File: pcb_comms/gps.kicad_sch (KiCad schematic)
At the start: 22 parts, among them U1 MAX-M10S-00B

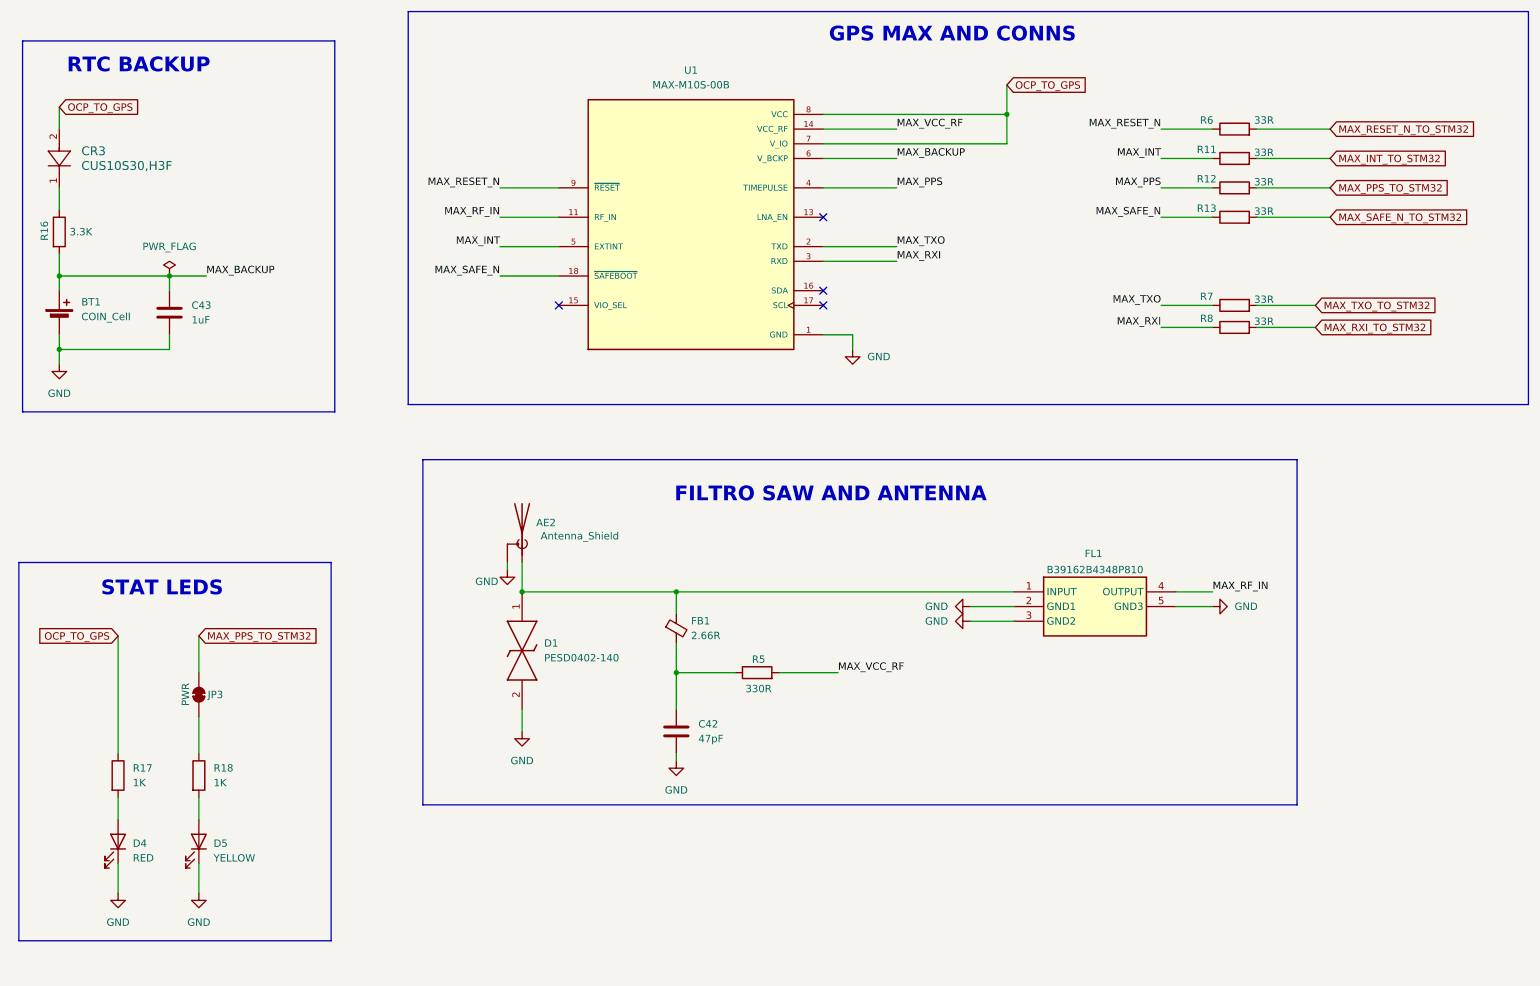
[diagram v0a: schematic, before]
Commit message: Add footprints
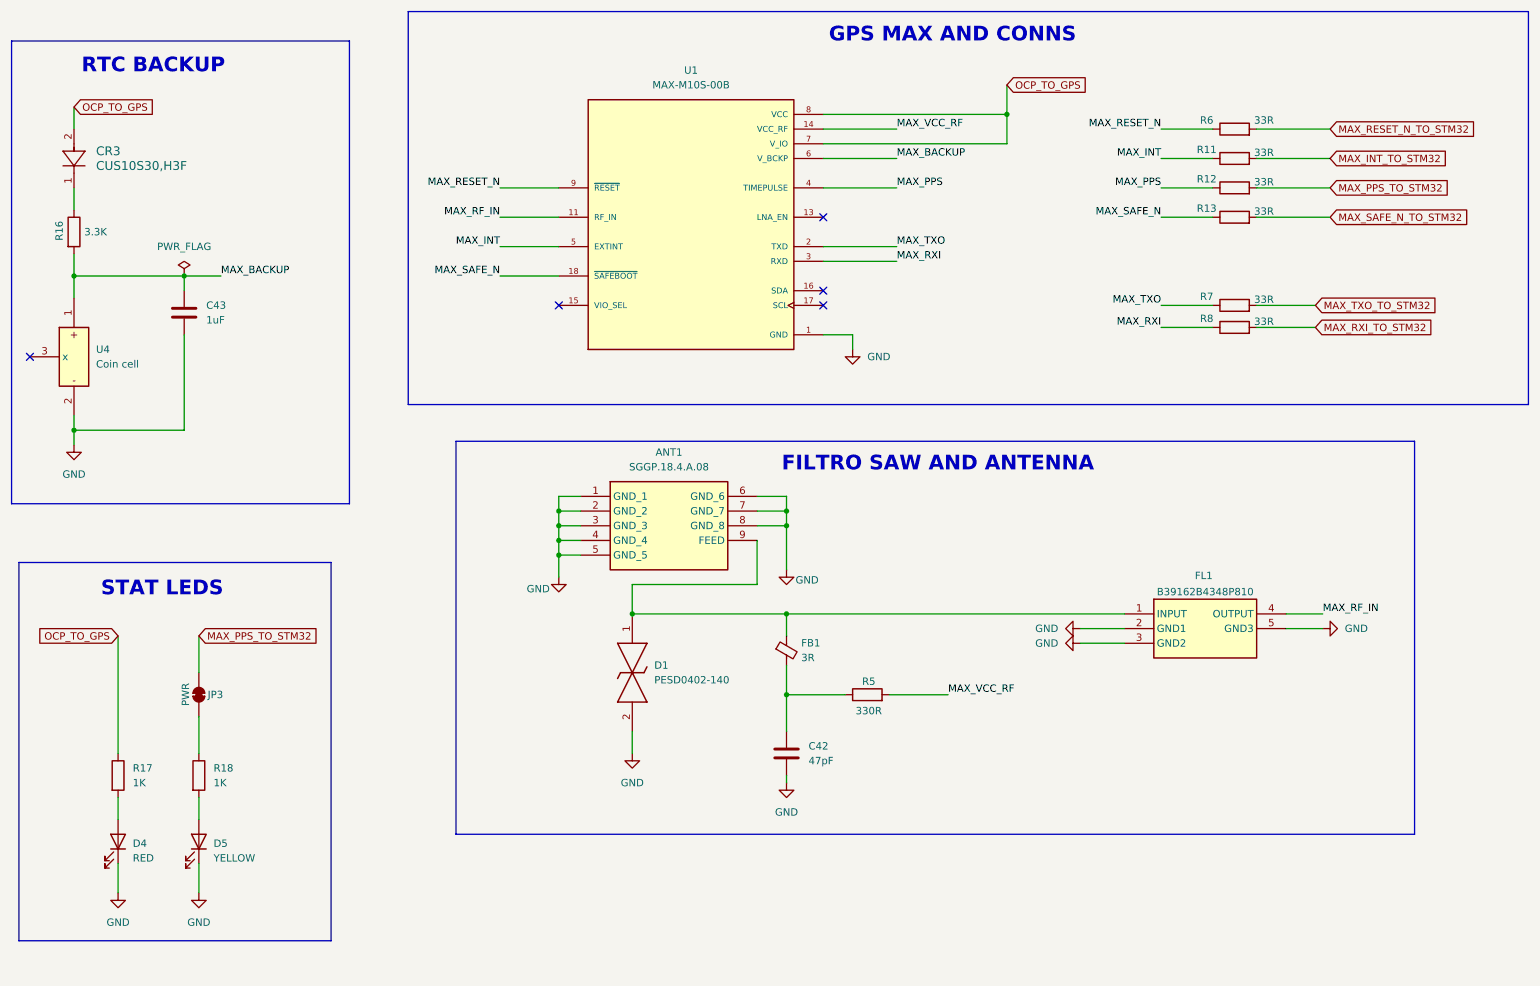
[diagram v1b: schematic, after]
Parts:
- removed AE2: Antenna_Shield, symbol Device:Antenna_Shield
- removed BT1: COIN_Cell, symbol Device:Battery_Cell
- added ANT1: SGGP.18.4.A.08, GPS_Antenna_SGGP.18.4.A.08:GPS_Antenna_SGGP.18.4.A.08, symbol GPS_Antenna_SGGP.18.4.A.08:SGGP.18.4.A.08
- added U4: Coin cell, GPS_BATTERY_HOLDER_2994:GPS_BATTERY_HOLDER_2994, symbol GPS_BATTERY_HOLDER_2994:2994TR
- C42, C43: footprint (none) -> Capacitor_SMD:C_0805_2012Metric_Pad1.18x1.45mm_HandSolder
- CR3: footprint (none) -> SCHOTTKY_DIODE_CUS10S30,H3F:SCHOTTKY_DIODE_CUS10S30,H3F
- D1: footprint (none) -> ESD_PROTECTION_DIODE_PESD0402-140:ESD_PROTECTION_DIODE_PESD0402-140
- D4, D5: footprint (none) -> LED_SMD:LED_0805_2012Metric_Pad1.15x1.40mm_HandSolder
- FB1: value 2.66R -> 3R; footprint (none) -> Inductor_SMD:L_0603_1608Metric_Pad1.05x0.95mm_HandSolder
- FL1: footprint (none) -> GPS_SAW_FILTER:B39162B4348P810
- JP3: footprint (none) -> Jumper:SolderJumper-2_P1.3mm_Bridged_RoundedPad1.0x1.5mm
- R11, R12, R13, R16, R17, R18, R5, R6, R7, R8: footprint (none) -> Resistor_SMD:R_0805_2012Metric_Pad1.20x1.40mm_HandSolder
- U1: footprint (none) -> GPS_MAX_M10S:XCVR_MAX-M10S-00B
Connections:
- net GND: now also ANT1.1 (GND_1), ANT1.2 (GND_2), ANT1.3 (GND_3), ANT1.4 (GND_4), ANT1.5 (GND_5), ANT1.6 (GND_6), ANT1.7 (GND_7), ANT1.8 (GND_8), U4.2
- net MAX_BACKUP: now also U4.1
- net at D1.1, FB1.1, FL1.1 (INPUT): now also ANT1.9 (FEED)
- no-connect marks 4 -> 5
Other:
- moved on the sheet: C42, C43, CR3, D1, FB1, FL1, R16, R5

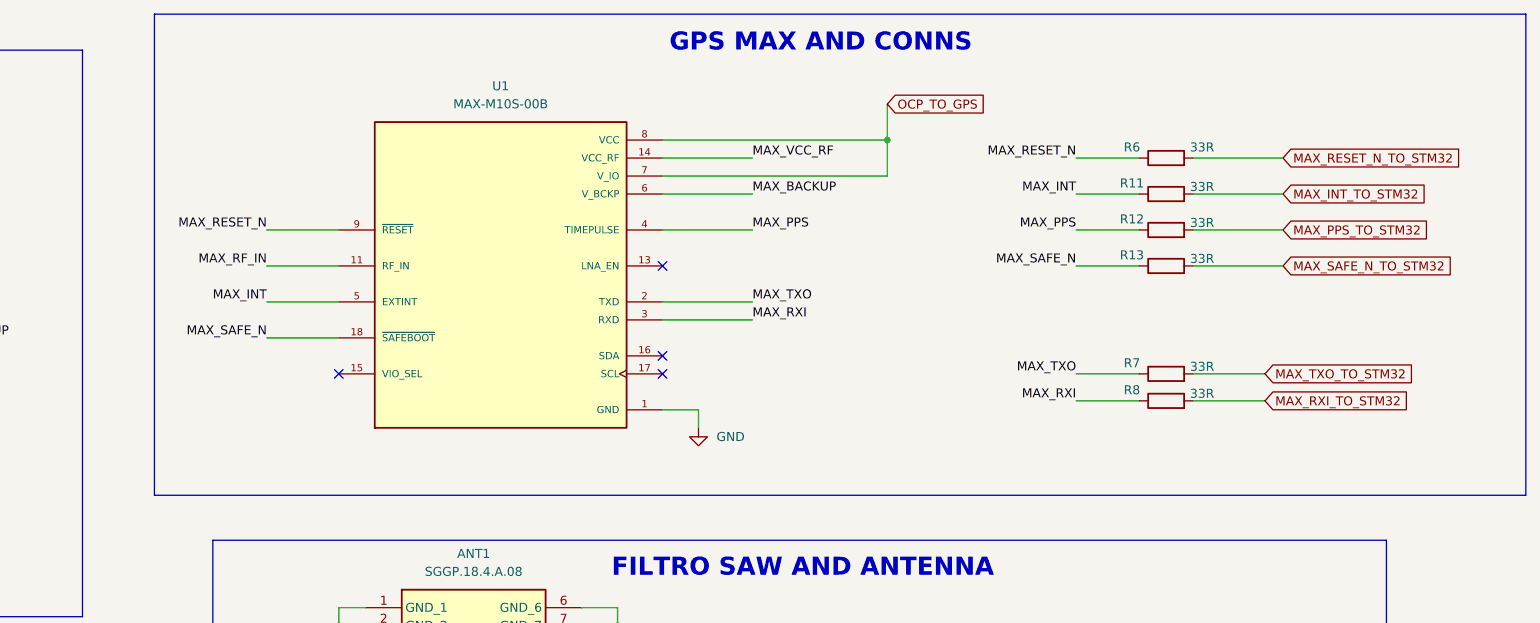
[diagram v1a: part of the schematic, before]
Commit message: Add DRA818
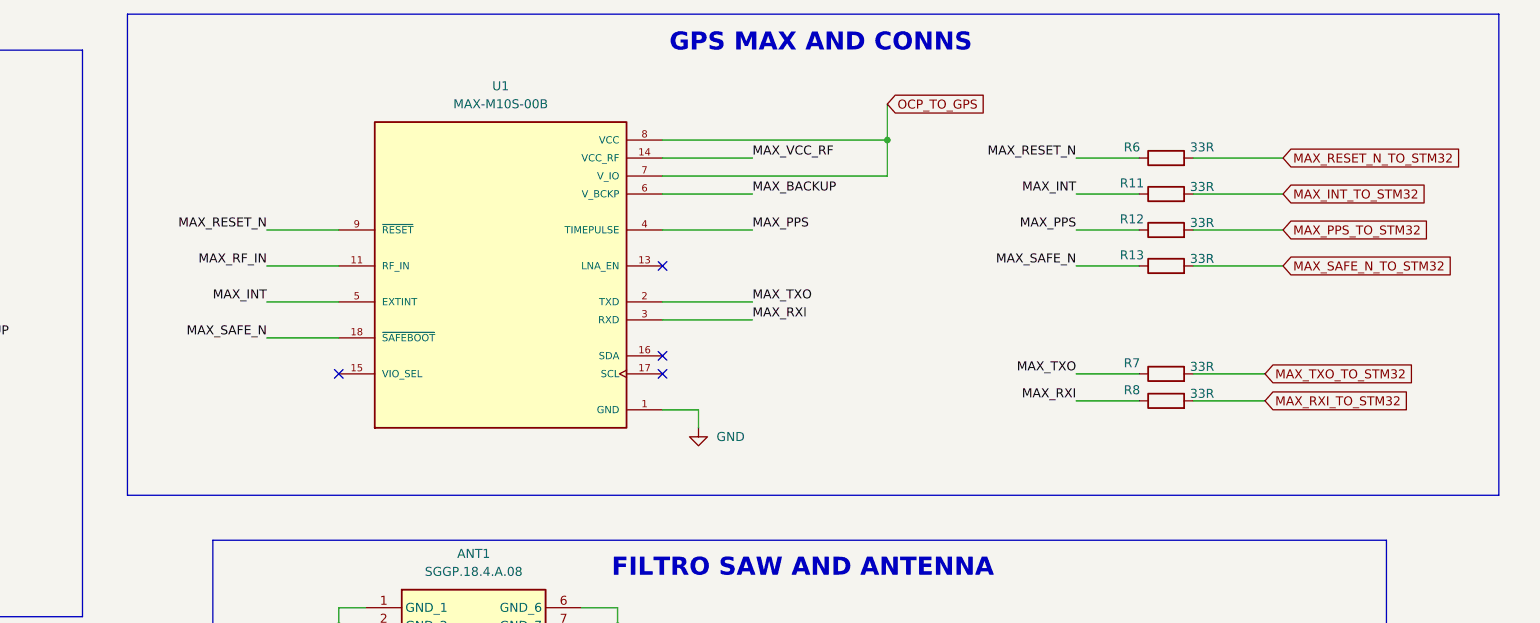
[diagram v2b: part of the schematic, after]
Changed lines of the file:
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@@
 	(text_box ""
 		(exclude_from_sim no)
-		(at 84.455 22.86 0)
+		(at 80.645 22.86 0)
 		(size 193.675 67.945)
 		(margins 0.9525 0.9525 0.9525 0.9525)

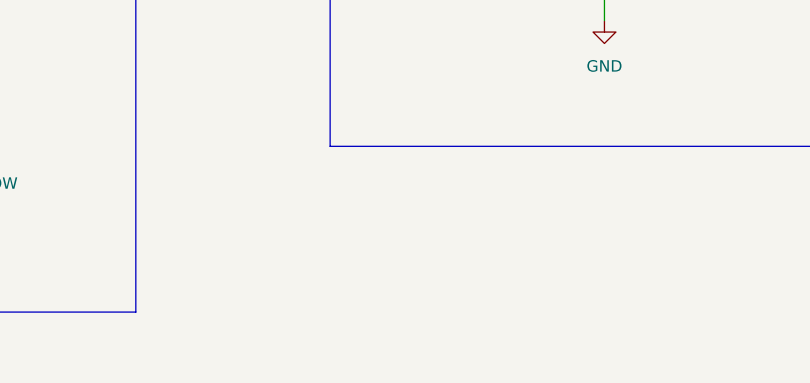
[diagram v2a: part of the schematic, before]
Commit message: remove gps
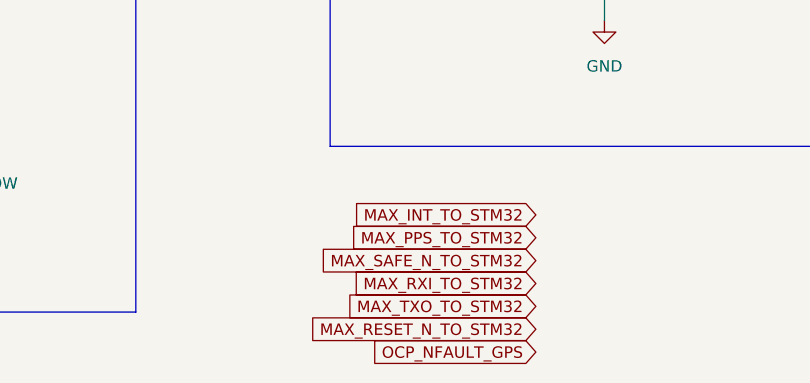
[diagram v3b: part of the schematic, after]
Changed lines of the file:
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@@
+		)
+	)
+	(global_label "MAX_PPS_TO_STM32"
+		(shape input)
+		(at 115.57 175.26 180)
+		(fields_autoplaced yes)
+		(effects
+			(font
+				(size 1.27 1.27)
+			)
+			(justify right)
+		)
+		(property "Intersheetrefs" "${INTERSHEET_REFS}"
+			(at 93.8374 175.26 0)
+			(effects
+				(font
+					(size 1.27 1.27)
+				)
+				(justify right)
+				(hide yes)
+			)
 		)
 	)
@@
 		)
 	)
+	(global_label "MAX_TXO_TO_STM32"
+		(shape input)
+		(at 115.57 182.88 180)
+		(fields_autoplaced yes)
+		(effects
+			(font
+				(size 1.27 1.27)
+			)
+			(justify right)
+		)
+		(property "Intersheetrefs" "${INTERSHEET_REFS}"
+			(at 94.0793 182.88 0)
+			(effects
+				(font
+					(size 1.27 1.27)
+				)
+				(justify right)
+				(hide yes)
+			)
+		)
+	)
 	(global_label "MAX_SAFE_N_TO_STM32"
 		(shape input)
@@
 	(global_label "MAX_RESET_N_TO_STM32"
 		(shape input)
+		(at 115.57 185.42 180)
+		(fields_autoplaced yes)
+		(effects
+			(font
+				(size 1.27 1.27)
+			)
+			(justify right)
+		)
+		(property "Intersheetrefs" "${INTERSHEET_REFS}"
+			(at 89.5437 185.42 0)
+			(effects
+				(font
+					(size 1.27 1.27)
+				)
+				(justify right)
+				(hide yes)
+			)
+		)
+	)
+	(global_label "MAX_RXI_TO_STM32"
+		(shape input)
+		(at 115.57 180.34 180)
+		(fields_autoplaced yes)
+		(effects
+			(font
+				(size 1.27 1.27)
+			)
+			(justify right)
+		)
+		(property "Intersheetrefs" "${INTERSHEET_REFS}"
+			(at 94.5026 180.34 0)
+			(effects
+				(font
+					(size 1.27 1.27)
+				)
+				(justify right)
+				(hide yes)
+			)
+		)
+	)
+	(global_label "MAX_RESET_N_TO_STM32"
+		(shape input)
 		(at 243.84 43.18 0)
 		(fields_autoplaced yes)
@@
 		)
 	)
+	(global_label "MAX_INT_TO_STM32"
+		(shape input)
+		(at 115.57 172.72 180)
+		(fields_autoplaced yes)
+		(effects
+			(font
+				(size 1.27 1.27)
+			)
+			(justify right)
+		)
+		(property "Intersheetrefs" "${INTERSHEET_REFS}"
+			(at 94.684 172.72 0)
+			(effects
+				(font
+					(size 1.27 1.27)
+				)
+				(justify right)
+				(hide yes)
+			)
+		)
+	)
+	(global_label "OCP_NFAULT_GPS"
+		(shape input)
+		(at 115.57 187.96 180)
+		(fields_autoplaced yes)
+		(effects
+			(font
+				(size 1.27 1.27)
+			)
+			(justify right)
+		)
+		(property "Intersheetrefs" "${INTERSHEET_REFS}"
+			(at 96.1957 187.96 0)
+			(effects
+				(font
+					(size 1.27 1.27)
+				)
+				(justify right)
+				(hide yes)
+			)
+		)
+	)
 	(global_label "OCP_TO_GPS"
 		(shape input)
@@
 				(hide yes)
 			)
+		)
+	)
+	(global_label "MAX_SAFE_N_TO_STM32"
+		(shape input)
+		(at 115.57 177.8 180)
+		(fields_autoplaced yes)
+		(effects
+			(font
+				(size 1.27 1.27)
+			)
+			(justify right)
+		)
+		(property "Intersheetrefs" "${INTERSHEET_REFS}"
+			(at 90.7531 177.8 0)
+			(effects
+				(font
+					(size 1.27 1.27)
+				)
+				(justify right)
+				(hide yes)
+			)
